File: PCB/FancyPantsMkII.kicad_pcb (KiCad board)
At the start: 2 copper layers, 65 x 48.5 mm, 13 parts, among them IC1 ATMEGA1284P-P, J1 J_SIGNAL, J2 J_DISPLAY, Y1 16MHz

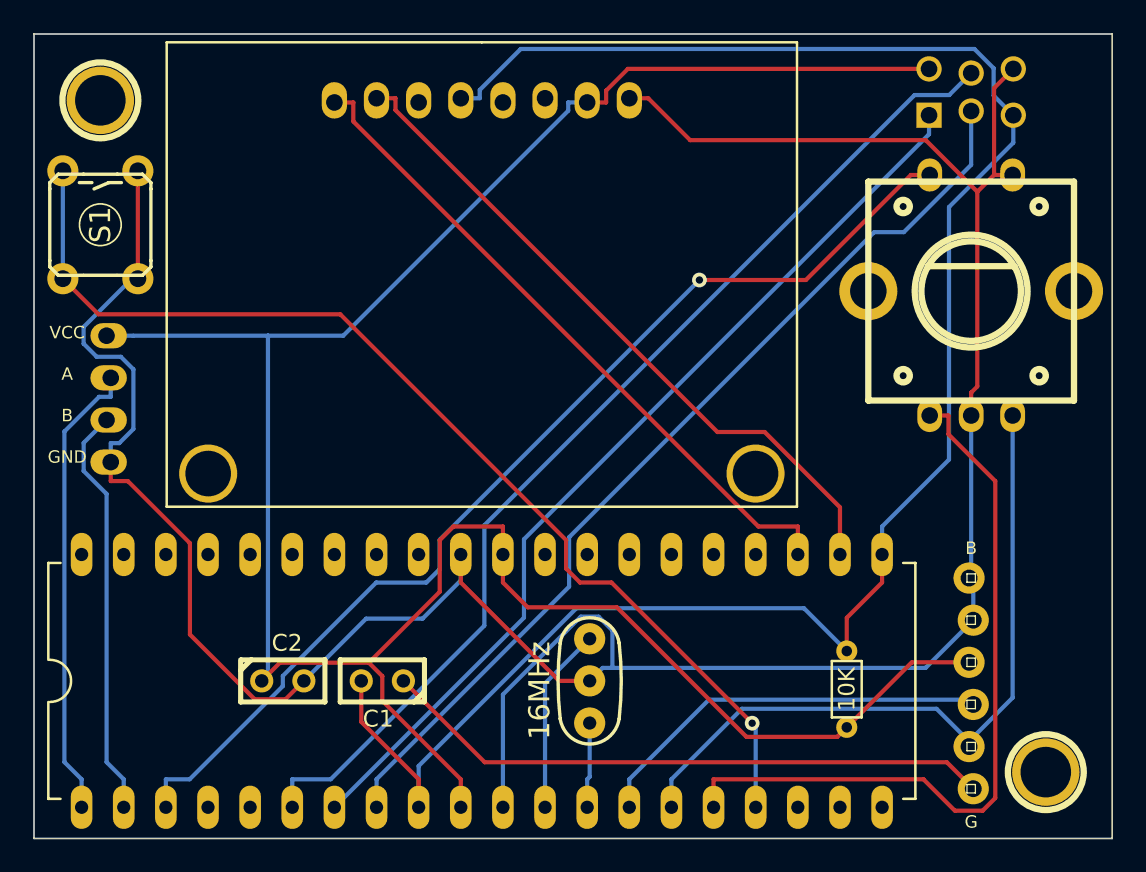
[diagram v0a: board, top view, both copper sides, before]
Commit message: fixed display reset net name
display reset net was named same as uC reset net, tying the two
together. Will probably never remake this board, but needed to fix the
net in case anyone else ever wants to.
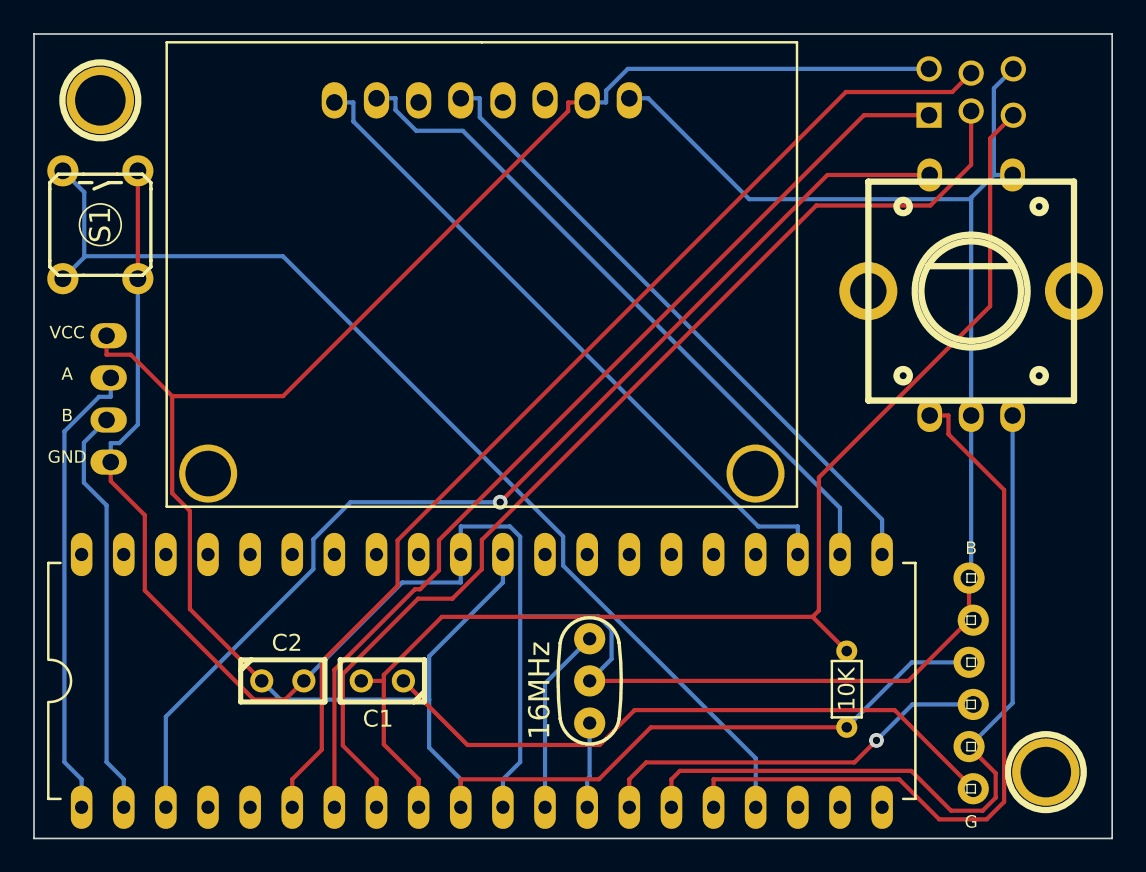
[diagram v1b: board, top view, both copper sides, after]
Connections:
- IC1 pad 21: RST -> DISP_RST
- J2 pad 4: RST -> DISP_RST
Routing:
- net RST: track 116.3 -> 75.7 mm
- net DISP_RST: track 0.00 -> 38.7 mm
- net SCK: track 57.9 -> 63.8 mm
- net ENC_B: track 43.3 -> 47.6 mm
- net 5VCC: track 146.4 -> 143.7 mm
- net MISO: track 56.6 -> 59.1 mm
- net GND: track 170.9 -> 168.5 mm
- net ENC_BTN: track 64.2 -> 66.1 mm
- net N-0000042: track 37.0 -> 38.8 mm
- net ENC_A: track 45.1 -> 46.5 mm
- net MOSI: track 63.8 -> 65.0 mm
- net BTN: track 65.3 -> 64.6 mm, vias 1 -> 0
- net TXO: track 24.5 -> 24.3 mm, vias 0 -> 1
